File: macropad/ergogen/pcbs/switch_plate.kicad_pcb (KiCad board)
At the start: 2 copper layers, 197 x 44.9 mm, 0 parts

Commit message: improvements
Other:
- outline, holes or cut-outs redrawn

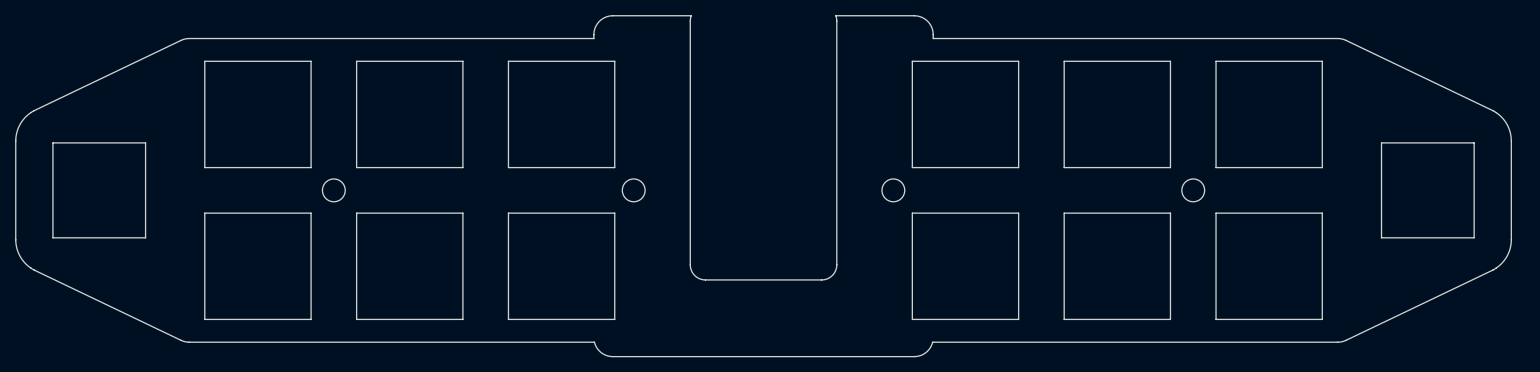
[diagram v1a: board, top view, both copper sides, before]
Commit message: Ajusting plate mcu cutout mcu is now a point of reference
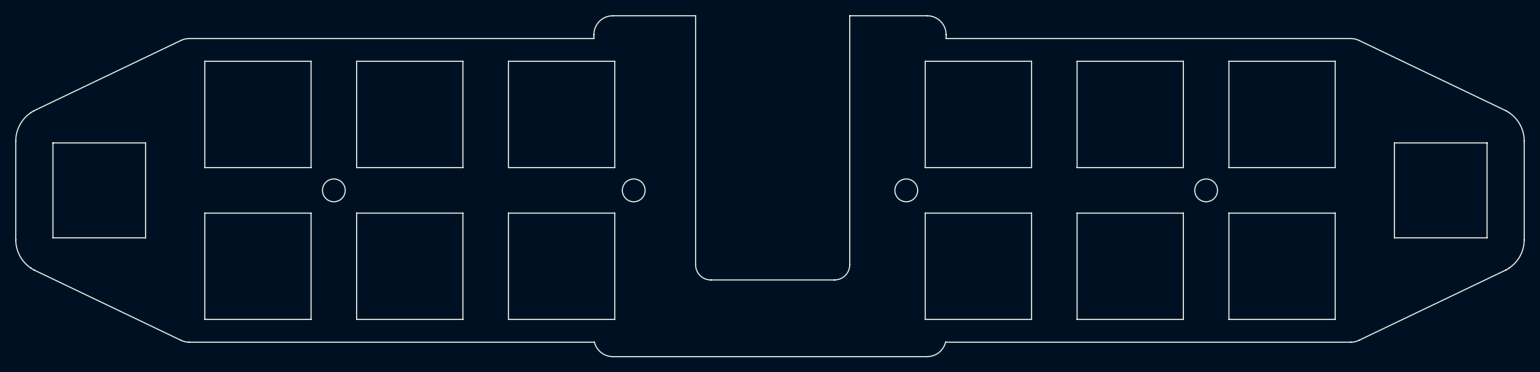
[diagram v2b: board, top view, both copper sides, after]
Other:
- board size 197 x 44.9 mm -> 198.7 x 44.9 mm
